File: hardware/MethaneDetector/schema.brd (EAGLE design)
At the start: 60.9 x 40.3 mm, 19 parts, among them IC1 AT90S2313P, Q1 2N4401, Q2 2N4401

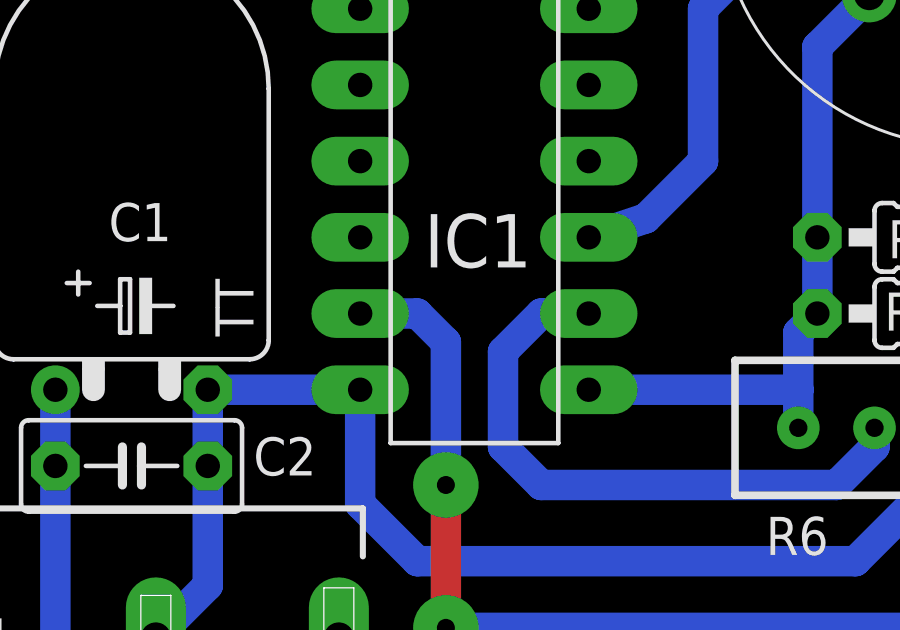
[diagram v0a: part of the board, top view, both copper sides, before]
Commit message: small component name fix
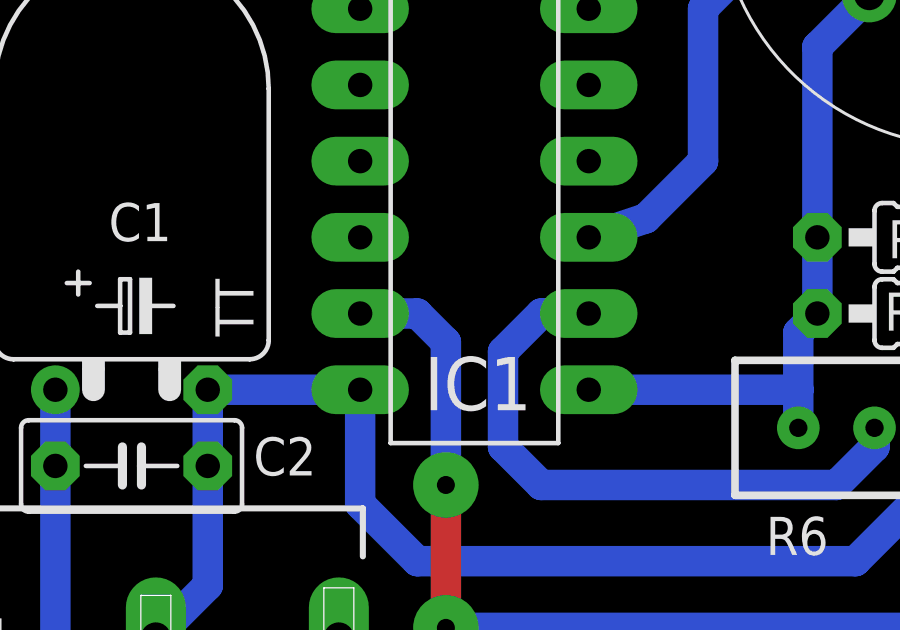
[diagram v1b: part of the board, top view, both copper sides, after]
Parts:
- IC1: value AT90S2313P -> ATtiny2313V-10PU
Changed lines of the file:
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@@
 <attribute name="VALUE" x="8.128" y="18.415" size="1.27" layer="27" ratio="10" rot="R90"/>
 </element>
-<element name="IC1" library="atmel" package="DIL20" value="AT90S2313P" x="17.78" y="25.4" smashed="yes" rot="R270">
+<element name="IC1" library="atmel" package="DIL20" value="ATtiny2313V-10PU" x="17.78" y="25.4" smashed="yes" rot="R270">
 <attribute name="OC_NEWARK" value="unknown" x="17.78" y="25.4" size="1.778" layer="27" rot="R270" display="off"/>
 <attribute name="MPN" value="" x="17.78" y="25.4" size="1.778" layer="27" rot="R270" display="off"/>
 <attribute name="OC_FARNELL" value="unknown" x="17.78" y="25.4" size="1.778" layer="27" rot="R270" display="off"/>
 <attribute name="MF" value="" x="17.78" y="25.4" size="1.778" layer="27" rot="R270" display="off"/>
-<attribute name="NAME" x="19.685" y="19.8247" size="1.778" layer="25" ratio="10" rot="R180"/>
-<attribute name="VALUE" x="17.018" y="35.56" size="1.778" layer="27" ratio="10" rot="R270"/>
+<attribute name="NAME" x="19.685" y="15.0622" size="1.778" layer="25" ratio="10" rot="R180"/>
+<attribute name="VALUE" x="17.018" y="38.1" size="1.778" layer="27" ratio="10" rot="R270"/>
 </element>
 <element name="LED1" library="adafruit" package="LED3MM" value="" x="55.88" y="22.86" smashed="yes" rot="R270">
